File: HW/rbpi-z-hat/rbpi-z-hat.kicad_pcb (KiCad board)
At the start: 2 copper layers, 65 x 30 mm, 69 parts, among them J1 Conn_02x20_Odd_Even, J2 Conn_01x10, J3 Conn_01x10, J4 Conn_01x10, J5 Conn_01x06, J6 Conn_01x06, J7 Conn_01x06, J8 Conn_01x06_MountingPin, Q1 DMG2302U, U1 MPU-9250, U2 MS5611, U3 PCA9685BS, U4 LSM9DS1, U5 BMP280, X1 ASEMB-25.000MHZ-LC-T

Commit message: Commit...
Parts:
- added C11: 22uF/16V, Capacitor_SMD:C_1210_3225Metric, F.Cu at (104.1, -23.9)
- added C18: 1uF/16V/NFM21PC105B1C3D, NFM21PC105B1C3D:NFM21PC105B1C3D, F.Cu at (103.8, -19.7)
- added C24: 0.1uF, Capacitor_SMD:C_0603_1608Metric, F.Cu at (117.8, -3.35)
- added C25: 0.1uF, Capacitor_SMD:C_0603_1608Metric, F.Cu at (118.7, -8.13)
- added C26: 10nF/16V, Capacitor_SMD:C_0603_1608Metric, F.Cu at (122.7, -8.13)
- added C27: 0.1uF, Capacitor_SMD:C_0603_1608Metric, F.Cu at (121.8, -5.62)
- added C28: 4.7uF, Capacitor_SMD:C_0805_2012Metric, F.Cu at (136.1, -20.4)
- added C29: 10nF, Capacitor_SMD:C_0603_1608Metric, F.Cu at (140.4, -24.7)
- added C30: 0.1uF, Capacitor_SMD:C_0603_1608Metric, F.Cu at (140.3, -20.7)
- added C31: 4.7uF/10V, Capacitor_SMD:C_0805_2012Metric, F.Cu at (90.5, 11.7)
- added C32: 10nF, Capacitor_SMD:C_0603_1608Metric, F.Cu at (95.6, 8.69)
- added C33: 100nF, Capacitor_SMD:C_0603_1608Metric, F.Cu at (98.7, 11.2)
- added C34: 0.1uF, Capacitor_SMD:C_0603_1608Metric, F.Cu at (99.6, 8.69)
- added C35: 22uF/10V, Capacitor_SMD:C_1206_3216Metric, F.Cu at (131.5, -9.38)
- added C36: 22uF/10V, Capacitor_SMD:C_1206_3216Metric, F.Cu at (131.5, -12.7)
- added D3: PESD0402-140, Diode_SMD:D_0402_1005Metric, F.Cu at (103.6, 0.36)
- added D4: PESD3V3S2UT, Package_TO_SOT_SMD:SOT-23, F.Cu at (101.0, -2.91)
- added D5: PESD0402-140, Diode_SMD:D_0402_1005Metric, F.Cu at (100.5, -13.6)
- added FB3: Ferrite_Bead, Inductor_SMD:L_0603_1608Metric, F.Cu at (95.9, -0.48)
- added FB4: Ferrite_Bead, Inductor_SMD:L_0603_1608Metric, F.Cu at (105.7, -8.13)
- added FB5: MPZ2012S221AT000, Inductor_SMD:L_0805_2012Metric, F.Cu at (101.0, -16.1)
- added FB6: MPZ2012S221AT000, Inductor_SMD:L_0805_2012Metric, F.Cu at (109.1, -24.5)
- added IC1: BQ24315DSGR, BQ24315DSGR:SON50P200X200X80-9N, F.Cu at (146.3, -13.6)
- added J10: JST_GH, Connector_JST:JST_GH_BM06B-GHS-TBT_1x06-1MP_P1.25mm_Vertical, F.Cu at (94.8, -22.1)
- added J9: JST_GH, Connector_JST:JST_GH_BM04B-GHS-TBT_1x04-1MP_P1.25mm_Vertical, F.Cu at (93.6, -5.56)
- added R10: 25K, Resistor_SMD:R_0603_1608Metric, F.Cu at (150.5, -12.0)
- added R11: 120, Resistor_SMD:R_0603_1608Metric, F.Cu at (99.6, 6.18)
- added R12: 10K, Resistor_SMD:R_0603_1608Metric, F.Cu at (94.7, 11.5)
- added R13: 10K, Resistor_SMD:R_0603_1608Metric, F.Cu at (95.6, 6.18)
- added R7: 10K/0.1%, Inductor_SMD:L_0603_1608Metric, F.Cu at (105.2, -13.8)
- added R8: 1M, Inductor_SMD:L_0603_1608Metric, F.Cu at (109.2, -18.0)
- added R9: 10K, Resistor_SMD:R_0603_1608Metric, F.Cu at (150.5, -14.5)
- added RN10: 10K/1%, Resistor_SMD:R_Array_Concave_4x0402, F.Cu at (108.8, -15.0)
- added RN9: 1K5, Resistor_SMD:R_Array_Concave_4x0402, F.Cu at (105.2, -5.10)
- added U10: MPU-9250, Package_DFN_QFN:QFN-24-1EP_3x3mm_P0.4mm_EP1.75x1.6mm, F.Cu at (91.0, 7.57)
- added U11: MIC5504-3.3YM5, Package_TO_SOT_SMD:SOT-23-5, F.Cu at (136.8, -12.0)
- added U6: ADS1015IDGS, Package_SO:TSSOP-10_3x3mm_P0.5mm, F.Cu at (118.9, -23.6)
- added U7: MIC5504-3.3YM5, Package_TO_SOT_SMD:SOT-23-5, F.Cu at (114.1, 7.25)
- added U8: LSM9DS1, Package_LGA:LGA-24L_3x3.5mm_P0.43mm, F.Cu at (114.1, -6.97)
- added U9: ICM-42688-P, Package_LGA:LGA-14_3x2.5mm_P0.5mm_LayoutBorder3x4y, F.Cu at (136.2, -23.9)
- C1: value 100nF -> 22uF/10V; footprint Capacitor_SMD:C_0603_1608Metric -> Capacitor_SMD:C_1206_3216Metric
- C17: value 100nF -> 22uF/16V; footprint Capacitor_SMD:C_0603_1608Metric -> Capacitor_SMD:C_1210_3225Metric
- C19: value 22uF/10V -> 1uF/16V/NFM21PC105B1C3D; footprint Capacitor_SMD:C_1206_3216Metric -> NFM21PC105B1C3D:NFM21PC105B1C3D
- C20, C21: value 0.1uF -> 22uF/10V; footprint Capacitor_SMD:C_0603_1608Metric -> Capacitor_SMD:C_1206_3216Metric
- C22: value 10nF/16V -> 100nF
- C23: value 0.1uF -> 4.7uF/10V; footprint Capacitor_SMD:C_0603_1608Metric -> Capacitor_SMD:C_0805_2012Metric
- C3: value 10nF -> 22uF/10V; footprint Capacitor_SMD:C_0603_1608Metric -> Capacitor_SMD:C_1206_3216Metric
- C5: value 100nF -> 1uF/16V/0805/NFM21PC105B1C3D; footprint Capacitor_SMD:C_0603_1608Metric -> NFM21PC105B1C3D:NFM21PC105B1C3D
- C6: value 22uF/10V -> 0.1uF; footprint Capacitor_SMD:C_1206_3216Metric -> Capacitor_SMD:C_0603_1608Metric
- C7: value 0.1uF -> 100nF
- J1: value Conn_02x20_Odd_Even -> RBPI_CONN
- R1: value 120 -> 200K
- R2: value 10K -> 10K/0.1%; footprint Resistor_SMD:R_0603_1608Metric -> Inductor_SMD:L_0603_1608Metric
- R3: value 10K -> 1M; footprint Resistor_SMD:R_0603_1608Metric -> Inductor_SMD:L_0603_1608Metric
- U1: value MPU-9250 -> MIC5504-3.3YM5; footprint Package_DFN_QFN:QFN-24-1EP_3x3mm_P0.4mm_EP1.75x1.6mm -> Package_TO_SOT_SMD:SOT-23-5
- U4: value LSM9DS1 -> PCA9306DC; footprint Package_LGA:LGA-24L_3x3.5mm_P0.43mm -> Package_SO:VSSOP-8_2.3x2mm_P0.5mm
- moved C22 131.2 mm to (155.6, -24.7)
- moved L11 121.7 mm to (151.6, -24.7), turned to 0 degrees
- moved L10 121.4 mm to (151.6, -22.2), turned to 0 degrees
- moved C7 116.8 mm to (128.4, -24.7), turned to 0 degrees
- moved C6 116.8 mm to (127.1, -22.2), turned to 0 degrees
- moved L4 115.1 mm to (124.4, -24.7), turned to 0 degrees
- moved U1 113.8 mm to (129.6, 3.99), turned to 0 degrees
- moved C10 113.5 mm to (118.3, -19.7), turned to 0 degrees
- moved L1 110.4 mm to (123.1, -20.1), turned to 0 degrees
- moved C1 107.1 mm to (124.3, 6.60), turned to 0 degrees
- moved C3 105.0 mm to (124.3, 3.31)
- moved R2 97.6 mm to (108.2, -20.5)
- moved R3 91.5 mm to (105.2, -16.3)
- moved C5 88.2 mm to (101.2, -7.28), turned to 0 degrees
- moved C23 83.7 mm to (113.6, -3.13)
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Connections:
- net /BARO/MS5611/MS_nCS renamed /BARO/BARO_MS_nCS
- C1 pad 1: +3V3 -> /BARO/MIC5504_BARO/MIC_VIN
- C1 pad 2: GNDD -> /BARO/BARO_FGND
- C10 pad 1: /BARO/BARO_VDD -> /ADS1015/ADS_VDD
- C10 pad 2: /BARO/BARO_GND -> /ADS1015/ADS_GND
- C12 pad 1: +3V3 -> /BARO/BARO_VIN
- C12 pad 2: GNDD -> /BARO/BARO_GND
- C17 pad 1: +3V3 -> /BQ24313/BQ_IN
- C19 pad 1: /LSM9DS1/LSM_VDD -> /POWER_CONN/BAT_VOLT
- C19 pad 2: /LSM9DS1/LSM_DGND -> GNDD
- C2 pad 2: /BARO/BARO_GND -> /BARO/BARO_FGND
- C20 pad 1: /LSM9DS1/LSM_VDD -> /BQ24313/BQ_OUT
- C20 pad 2: /LSM9DS1/LSM_DGND -> /MIC5504/MIC_GND
- C21 pad 1: /LSM9DS1/LSM_VDD -> /MIC5504/MIC_VOUT
- C21 pad 2: /LSM9DS1/LSM_DGND -> /MIC5504/MIC_GND
- C22 pad 1: Net-(C22-Pad1) -> /IMU/IMU_VIN
- C22 pad 2: /LSM9DS1/LSM_DGND -> /IMU/IMU_GND
- C23 pad 1: Net-(C23-Pad1) -> /IMU/IMU_VDD
- C23 pad 2: /LSM9DS1/LSM_DGND -> /IMU/IMU_FGND
- C3 pad 1: Net-(C3-Pad1) -> /BARO/BARO_VDD
- C3 pad 2: /MPU9250/MPU_FGND -> /BARO/BARO_FGND
- C4 pad 2: /BARO/BARO_GND -> /BARO/BARO_FGND
- C5 pad 1: Net-(C3-Pad1) -> Net-(C5-Pad1)
- C5 pad 2: /MPU9250/MPU_FGND -> GNDD
- C6 pad 1: Net-(C3-Pad1) -> GNDD
- C6 pad 2: /MPU9250/MPU_FGND -> /ADS1015/ADS_VDD
- C7 pad 1: /MPU9250/MPU_FGND -> +3V3
- C7 pad 2: Net-(C7-Pad2) -> GNDD
- C9 pad 2: /BARO/BARO_GND -> /BARO/BARO_FGND
- J1 pad 11: (no net) -> /rbpi/UART_CTS
- J1 pad 12: (no net) -> /rbpi/UART_RTS
- J1 pad 19: /rbpi/SPI0_MOSI -> /rbpi/SPI1_MOSI
- J1 pad 21: /rbpi/SPI0_MISO -> /rbpi/SPI1_MISO
- J1 pad 23: /rbpi/SPI0_SCLK -> /rbpi/SPI1_SCLK
- J1 pad 24: /rbpi/SPI0_CE0 -> (no net)
- J1 pad 3: /rbpi/SDA1 -> (no net)
- J1 pad 35: /rbpi/SPI1_MISO -> (no net)
- J1 pad 36: /rbpi/SPI1_CE2 -> (no net)
- J1 pad 38: /rbpi/SPI1_MOSI -> (no net)
- J1 pad 40: /rbpi/SPI1_SCLK -> (no net)
- J1 pad 5: /rbpi/SCL1 -> (no net)
- J1 pad 7: /rbpi/GPIO_4 -> (no net)
- L1 pad 2: Net-(C3-Pad1) -> /ADS1015/ADS_VDD
- L10 pad 1: +3V3 -> /IMU/IMU_VIN
- L10 pad 2: /LSM9DS1/LSM_VDD -> /IMU/MIC5504_IMU/MIC_VIN
- L11 pad 1: GNDD -> /IMU/IMU_GND
- L11 pad 2: /LSM9DS1/LSM_DGND -> /IMU/IMU_FGND
- L2 pad 1: +3V3 -> /BARO/BARO_VIN
- L2 pad 2: /BARO/BARO_VDD -> /BARO/MIC5504_BARO/MIC_VIN
- L3 pad 1: GNDD -> /BARO/BARO_GND
- L3 pad 2: /BARO/BARO_GND -> /BARO/BARO_FGND
- L4 pad 2: /MPU9250/MPU_FGND -> /ADS1015/ADS_GND
- R1 pad 1: (no net) -> Net-(R1-Pad1)
- R1 pad 2: Net-(R1-Pad2) -> +3V3
- R2 pad 1: /MPU9250/MPU_MISO -> Net-(C18-Pad3)
- R2 pad 2: /MPU9250/MPU_FGND -> Net-(R2-Pad2)
- R3 pad 1: Net-(R3-Pad1) -> /POWER_CONN/BAT_CUR
- R3 pad 2: /MPU9250/MPU_FGND -> GNDD
- R6 pad 1: /rbpi/GPIO_4 -> (no net)
- RN5 pad 3: /rbpi/SCL1 -> /rbpi/UART_CTS
- RN5 pad 4: /rbpi/SDA1 -> /rbpi/UART_RTS
- RN6 pad 1: /rbpi/SPI0_MOSI -> (no net)
- RN6 pad 2: /rbpi/SPI0_MISO -> (no net)
- RN6 pad 3: /rbpi/SPI0_SCLK -> (no net)
- RN6 pad 4: /rbpi/SPI0_CE0 -> (no net)
- RN7 pad 1: /rbpi/SPI1_MISO -> /rbpi/SPI1_MOSI
- RN7 pad 2: /rbpi/SPI1_CE2 -> /rbpi/SPI1_MISO
- RN7 pad 3: /rbpi/SPI1_MOSI -> /rbpi/SPI1_SCLK
- RN7 pad 4: /rbpi/SPI1_SCLK -> (no net)
- U1 pad 1: Net-(C3-Pad1) -> /BARO/MIC5504_BARO/MIC_VIN
- U1 pad 2: (no net) -> /BARO/BARO_FGND
- U1 pad 5: (no net) -> /BARO/BARO_VDD
- U2 pad 2: /BARO/BARO_GND -> /BARO/BARO_FGND
- U2 pad 3: /BARO/BARO_GND -> /BARO/BARO_FGND
- U2 pad 6: (no net) -> /BARO/BARO_MISO
- U2 pad 7: (no net) -> /BARO/BARO_MOSI
- U2 pad 8: (no net) -> /BARO/BARO_SCK
- U4 pad 1: /LSM9DS1/LSM_VDD -> +3V3
- U4 pad 2: (no net) -> /I2C_CONN/SCL
- U4 pad 3: /LSM9DS1/LSM_VDD -> /I2C_CONN/SDA
- U4 pad 4: (no net) -> GNDD
- U4 pad 5: /LSM9DS1/LSM_MISO -> Net-(D4-Pad1)
- U4 pad 6: /LSM9DS1/LSM_MISO -> Net-(D4-Pad2)
- U4 pad 7: /LSM9DS1/LSM_nCS -> Net-(R1-Pad1)
- U4 pad 8: /LSM9DS1/LSM_nCS -> Net-(R1-Pad1)
- U5 pad 1: /BARO/BARO_GND -> /BARO/BARO_FGND
- U5 pad 3: (no net) -> /BARO/BARO_MOSI
- U5 pad 4: (no net) -> /BARO/BARO_SCK
- U5 pad 5: (no net) -> /BARO/BARO_MISO
- U5 pad 7: /BARO/BARO_GND -> /BARO/BARO_FGND

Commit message: Commit
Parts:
- IC1: footprint BQ24315DSGR:SON50P200X200X80-9N -> SON50P200X200X80-9N
- RN5, RN6, RN7: value 47K/4x0603 -> 10K/4x0402
- moved U1 127.9 mm to (9.32, 47.7), turned to 270 degrees
- moved C3 124.5 mm to (9.32, 51.0), turned to 180 degrees
- moved R2 121.5 mm to (-8.22, 14.2), turned to 90 degrees
- moved C1 121.0 mm to (9.32, 44.4), turned to 180 degrees
- moved R8 119.9 mm to (-4.21, 20.7)
- moved R3 118.6 mm to (-7.45, 20.7)
- moved C18 118.1 mm to (-8.25, 17.8), turned to 90 degrees
- moved RN10 117.8 mm to (-6.06, 11.6), turned to 90 degrees
- moved R7 113.7 mm to (-4.98, 14.2), turned to 90 degrees
- moved FB6 109.6 mm to (9.97, 22.2)
- moved C19 106.9 mm to (-4.98, 17.8), turned to 90 degrees
- moved D2 98.4 mm to (-20.0, 29.2), turned to 180 degrees
- moved J8 97.6 mm to (-19.5, 29.3), turned to 90 degrees
- moved C11 97.5 mm to (17.1, 20.0)
- moved J10 95.5 mm to (12.8, 26.8), turned to 180 degrees
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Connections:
- net /rbpi/SPI1_MISO renamed /rbpi/SPI0_MISO
- net /rbpi/SPI1_MOSI renamed /rbpi/SPI0_MOSI
- net /rbpi/SPI1_SCLK renamed /rbpi/SPI0_SCLK
- C35 pad 2: /IMU/MIC5504_IMU/MIC_GND -> /IMU/IMU_FGND
- C36 pad 2: /IMU/MIC5504_IMU/MIC_GND -> /IMU/IMU_FGND
- C6 pad 1: GNDD -> /ADS1015/ADS_GND
- J1 pad 11: /rbpi/UART_CTS -> (no net)
- J1 pad 12: /rbpi/UART_RTS -> (no net)
- J1 pad 24: (no net) -> /rbpi/SPI1_CE2
- J1 pad 3: (no net) -> /rbpi/SCL1
- J1 pad 5: (no net) -> /rbpi/SDA1
- J1 pad 7: (no net) -> /rbpi/Pin_7_PPM_SBUS_INPUT
- RN5 pad 3: /rbpi/UART_CTS -> (no net)
- RN5 pad 4: /rbpi/UART_RTS -> (no net)
- RN6 pad 1: (no net) -> /rbpi/SCL1
- RN6 pad 2: (no net) -> /rbpi/SDA1
- RN6 pad 3: (no net) -> /rbpi/Pin_7_PPM_SBUS_INPUT
- RN6 pad 6: +3V3 -> (no net)
- RN7 pad 4: (no net) -> /rbpi/SPI1_CE2
- U11 pad 2: /IMU/MIC5504_IMU/MIC_GND -> /IMU/IMU_FGND

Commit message: Commit...
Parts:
- removed Q1: DMG2302U, Package_TO_SOT_SMD:SOT-23
- C11, C17, D4, FB5: moved to B.Cu
- moved FB1 32.8 mm to (12.8, 17.4), turned to 90 degrees
- moved C8 28.0 mm to (10.0, 18.2), turned to 180 degrees
- moved J8 27.1 mm to (3.50, 15.0)
- moved D1 27.1 mm to (7.49, 18.7)
- moved RN8 27.0 mm to (8.00, 15.0)
- moved FB2 26.9 mm to (7.75, 11.0), turned to 270 degrees
- moved D2 26.8 mm to (2.67, 15.0)
- moved C17 11.0 mm to (14.0, 27.1), turned to 270 degrees
- moved L5 8.96 mm to (-10.9, 5.08)
- moved L6 8.96 mm to (-9.14, 5.08)
- moved L7 8.96 mm to (-10.9, 1.86)
- moved L8 8.96 mm to (-9.14, 1.86)
- moved C11 7.12 mm to (17.5, 27.1), turned to 270 degrees
- moved D4 6.16 mm to (24.4, 27.6), turned to 270 degrees
- moved FB5 5.79 mm to (15.8, 23.7), turned to 0 degrees
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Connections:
- net /rbpi/SCL1 renamed /SCL1
- net /rbpi/SDA1 renamed /SDA1
- J1 pad 10: /rbpi/UART_RX -> /UART_RX
- J1 pad 8: /rbpi/UART_TX -> /UART_TX
- RN10 pad 5: /POWER_CONN/BAT_CUR_SENS -> /CUR_SENS
- RN10 pad 6: /POWER_CONN/BAT_VOLT_SENS -> /VOLT_SENS
- RN10 pad 7: /POWER_CONN/BAT_VOLT_SENS -> /VOLT_SENS
- RN10 pad 8: /POWER_CONN/BAT_CUR_SENS -> /CUR_SENS
- RN5 pad 1: /rbpi/UART_RX -> /UART_RX
- RN5 pad 2: /rbpi/UART_TX -> /UART_TX
- RN5 pad 3: (no net) -> /UART_CTS
- RN5 pad 4: (no net) -> /UART_RTS
- RN8 pad 1: (no net) -> /UART_TX
- RN8 pad 2: (no net) -> /UART_RX
- RN8 pad 3: (no net) -> /UART_CTS
- RN8 pad 4: (no net) -> /UART_RTS
- U6 pad 4: (no net) -> /CUR_SENS
- U6 pad 5: (no net) -> /VOLT_SENS

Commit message: Commit..
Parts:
- moved C22 113.5 mm to (24.1, -31.6)
- moved C35 113.5 mm to (24.0, -26.2)
- moved C36 113.5 mm to (24.0, -19.3)
- moved L11 113.5 mm to (23.2, -29.1)
- moved U11 113.5 mm to (24.0, -22.7)
- moved L10 113.5 mm to (25.0, -29.1)
- moved C33 82.3 mm to (50.9, -23.9)
- moved C34 82.3 mm to (46.5, -20.1)
- moved R11 82.3 mm to (50.0, -20.1)
- moved C31 82.3 mm to (51.1, -26.0)
- moved C32 82.3 mm to (42.9, -20.1)
- moved R12 82.3 mm to (44.7, -20.1)
- moved R13 82.3 mm to (48.3, -20.1)
- moved U10 82.3 mm to (46.4, -24.9)
- moved C29 81.2 mm to (49.9, -33.8)
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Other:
- copper layers 2 -> 4

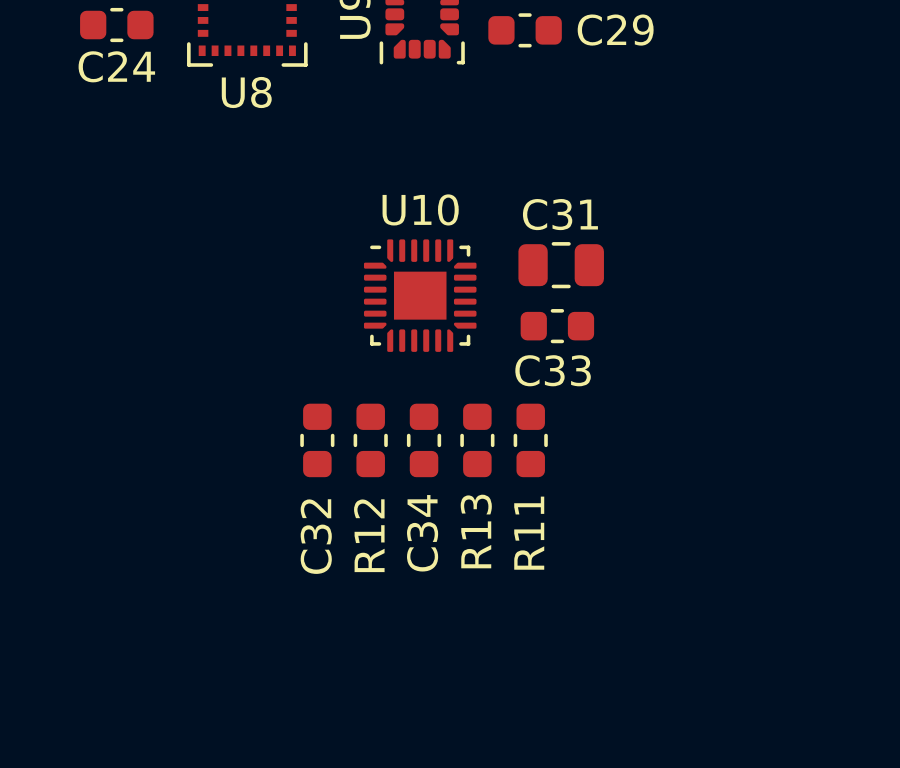
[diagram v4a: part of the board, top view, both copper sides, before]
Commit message: Removed MPU-9250
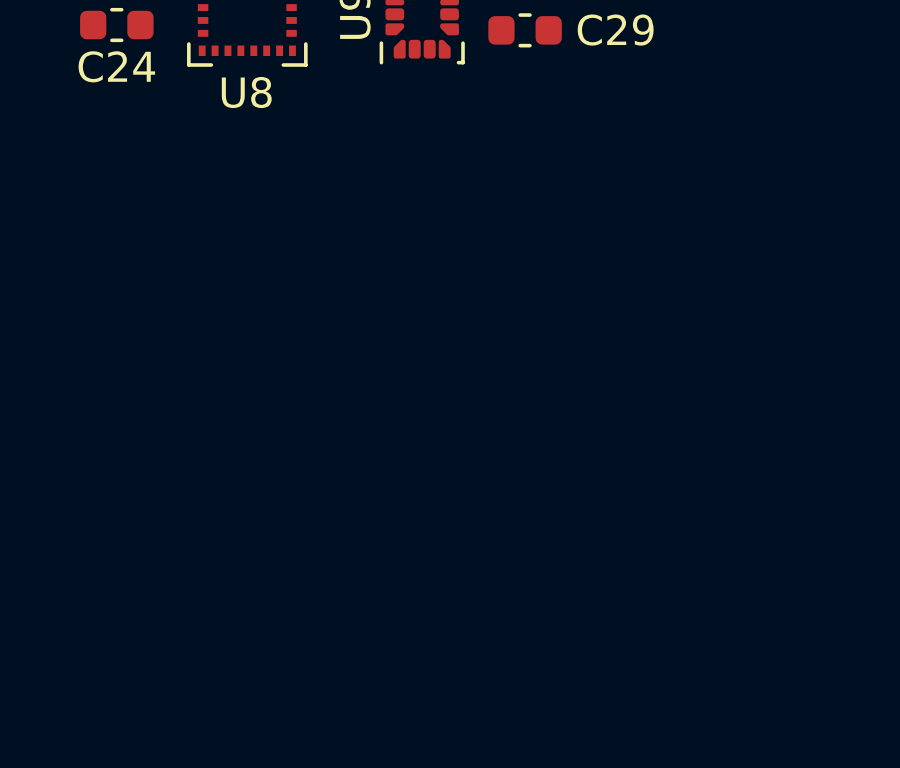
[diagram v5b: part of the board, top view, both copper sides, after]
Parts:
- removed C31: 4.7uF/10V, Capacitor_SMD:C_0805_2012Metric
- removed C32: 10nF, Capacitor_SMD:C_0603_1608Metric
- removed C33: 100nF, Capacitor_SMD:C_0603_1608Metric
- removed C34: 0.1uF, Capacitor_SMD:C_0603_1608Metric
- removed R11: 120, Resistor_SMD:R_0603_1608Metric
- removed R12, R13: 10K, Resistor_SMD:R_0603_1608Metric
- removed U10: MPU-9250, Package_DFN_QFN:QFN-24-1EP_3x3mm_P0.4mm_EP1.75x1.6mm

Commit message: Commit
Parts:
- moved C23 50.7 mm to (23.8, 10.1)
- moved C24 50.7 mm to (22.5, 14.8)
- moved C25 50.7 mm to (25.8, 10.2)
- moved C26 50.7 mm to (27.5, 10.2)
- moved C27 50.7 mm to (22.5, 13.2)
- moved C28 50.7 mm to (36.4, 13.0)
- moved C29 50.7 mm to (36.1, 15.0)
- moved C30 50.7 mm to (33.5, 10.7)
- moved U8 50.7 mm to (26.9, 14.4)
- moved U9 50.7 mm to (32.7, 14.5)

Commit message: Commit
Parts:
- moved C23 35.9 mm to (39.0, -22.4)
- moved C24 35.9 mm to (37.8, -17.7)
- moved C25 35.9 mm to (41.1, -22.3)
- moved C26 35.9 mm to (42.7, -22.3)
- moved C27 35.9 mm to (37.8, -19.4)
- moved C28 35.9 mm to (51.6, -19.6)
- moved C29 35.9 mm to (51.4, -17.5)
- moved C30 35.9 mm to (48.7, -21.8)
- moved U8 35.9 mm to (42.1, -18.1)
- moved U9 35.9 mm to (48.0, -18.1)

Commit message: Commit
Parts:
- removed C35, C36: 22uF/10V, Capacitor_SMD:C_1206_3216Metric
- removed L10, L11: Ferrite_Bead, Inductor_SMD:L_0603_1608Metric
- removed U11: MIC5504-3.3YM5, Package_TO_SOT_SMD:SOT-23-5
- added C31: 22uF/10V, Capacitor_SMD:C_1206_3216Metric, F.Cu at (87.3, 17.4)
- C22: value 100nF -> 22uF/10V; footprint Capacitor_SMD:C_0603_1608Metric -> Capacitor_SMD:C_1206_3216Metric
- moved L3 101.5 mm to (106.0, 13.8), turned to 0 degrees
- moved C12 96.0 mm to (102.0, 13.8), turned to 0 degrees
- moved C1 95.9 mm to (102.8, 22.6), turned to 0 degrees
- moved L2 95.0 mm to (102.0, 16.3), turned to 0 degrees
- moved U1 89.5 mm to (92.5, 14.8), turned to 0 degrees
- moved C3 82.5 mm to (87.3, 24.1), turned to 0 degrees
- moved C22 78.0 mm to (87.3, 14.1), turned to 0 degrees
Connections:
- net /BARO/BARO_GND renamed /SENSORS_POWER/SENS_GND
- net /BARO/BARO_VIN renamed /SENSORS_POWER/SENS_VIN
- C1 pad 1: /BARO/MIC5504_BARO/MIC_VIN -> /SENS_VDD
- C1 pad 2: /BARO/BARO_FGND -> /SENS_FGND
- C2 pad 1: /BARO/BARO_VDD -> /SENS_VDD
- C2 pad 2: /BARO/BARO_FGND -> /SENS_FGND
- C22 pad 1: /IMU/IMU_VIN -> /SENSORS_POWER/sheet5EE7A825/MIC_VIN
- C22 pad 2: /IMU/IMU_GND -> /SENS_FGND
- C23 pad 1: /IMU/IMU_VDD -> /SENS_VDD
- C23 pad 2: /IMU/IMU_FGND -> /SENS_FGND
- C24 pad 1: /IMU/IMU_VDD -> /SENS_VDD
- C24 pad 2: /IMU/IMU_FGND -> /SENS_FGND
- C25 pad 1: /IMU/IMU_VDD -> /SENS_VDD
- C25 pad 2: /IMU/IMU_FGND -> /SENS_FGND
- C26 pad 2: /IMU/IMU_FGND -> /SENS_FGND
- C27 pad 2: /IMU/IMU_FGND -> /SENS_FGND
- C28 pad 1: /IMU/IMU_VDD -> /SENS_VDD
- C28 pad 2: /IMU/IMU_FGND -> /SENS_FGND
- C29 pad 1: /IMU/IMU_VDD -> /SENS_VDD
- C29 pad 2: /IMU/IMU_FGND -> /SENS_FGND
- C3 pad 1: /BARO/BARO_VDD -> /SENS_VDD
- C3 pad 2: /BARO/BARO_FGND -> /SENS_FGND
- C30 pad 1: /IMU/IMU_VDD -> /SENS_VDD
- C30 pad 2: /IMU/IMU_FGND -> /SENS_FGND
- C4 pad 1: /BARO/BARO_VDD -> /SENS_VDD
- C4 pad 2: /BARO/BARO_FGND -> /SENS_FGND
- C9 pad 1: /BARO/BARO_VDD -> /SENS_VDD
- C9 pad 2: /BARO/BARO_FGND -> /SENS_FGND
- L2 pad 2: /BARO/MIC5504_BARO/MIC_VIN -> /SENSORS_POWER/sheet5EE7A825/MIC_VIN
- L3 pad 2: /BARO/BARO_FGND -> /SENS_FGND
- RN9 pad 3: /I2C_CONN/SDA -> /SDA1
- RN9 pad 4: /I2C_CONN/SCL -> /SCL1
- U1 pad 1: /BARO/MIC5504_BARO/MIC_VIN -> /SENSORS_POWER/sheet5EE7A825/MIC_VIN
- U1 pad 2: /BARO/BARO_FGND -> /SENS_FGND
- U1 pad 5: /BARO/BARO_VDD -> /SENS_VDD
- U2 pad 1: /BARO/BARO_VDD -> /SENS_VDD
- U2 pad 2: /BARO/BARO_FGND -> /SENS_FGND
- U2 pad 3: /BARO/BARO_FGND -> /SENS_FGND
- U3 pad 23: (no net) -> /SCL1
- U3 pad 24: (no net) -> /SDA1
- U4 pad 2: /I2C_CONN/SCL -> /SCL1
- U4 pad 3: /I2C_CONN/SDA -> /SDA1
- U5 pad 1: /BARO/BARO_FGND -> /SENS_FGND
- U5 pad 6: /BARO/BARO_VDD -> /SENS_VDD
- U5 pad 7: /BARO/BARO_FGND -> /SENS_FGND
- U5 pad 8: /BARO/BARO_VDD -> /SENS_VDD
- U8 pad 1: /IMU/IMU_VDD -> /SENS_VDD
- U8 pad 14: /IMU/IMU_FGND -> /SENS_FGND
- U8 pad 15: /IMU/IMU_FGND -> /SENS_FGND
- U8 pad 16: /IMU/IMU_FGND -> /SENS_FGND
- U8 pad 17: /IMU/IMU_FGND -> /SENS_FGND
- U8 pad 18: /IMU/IMU_FGND -> /SENS_FGND
- U8 pad 19: /IMU/IMU_FGND -> /SENS_FGND
- U8 pad 20: /IMU/IMU_FGND -> /SENS_FGND
- U8 pad 22: /IMU/IMU_VDD -> /SENS_VDD
- U8 pad 23: /IMU/IMU_VDD -> /SENS_VDD
- U8 pad 3: /IMU/IMU_VDD -> /SENS_VDD
- U9 pad 5: /IMU/IMU_VDD -> /SENS_VDD
- U9 pad 6: /IMU/IMU_FGND -> /SENS_FGND
- U9 pad 8: /IMU/IMU_VDD -> /SENS_VDD
